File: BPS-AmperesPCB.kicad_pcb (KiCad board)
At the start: 2 copper layers, 58.2 x 30.2 mm, 32 parts, among them J1 ShuntConn, J2 LeaderConn, U1 AS8510-ASSM, U2 RO-123.3S_HP, U3 LTC6820, U4 HX1188FNL

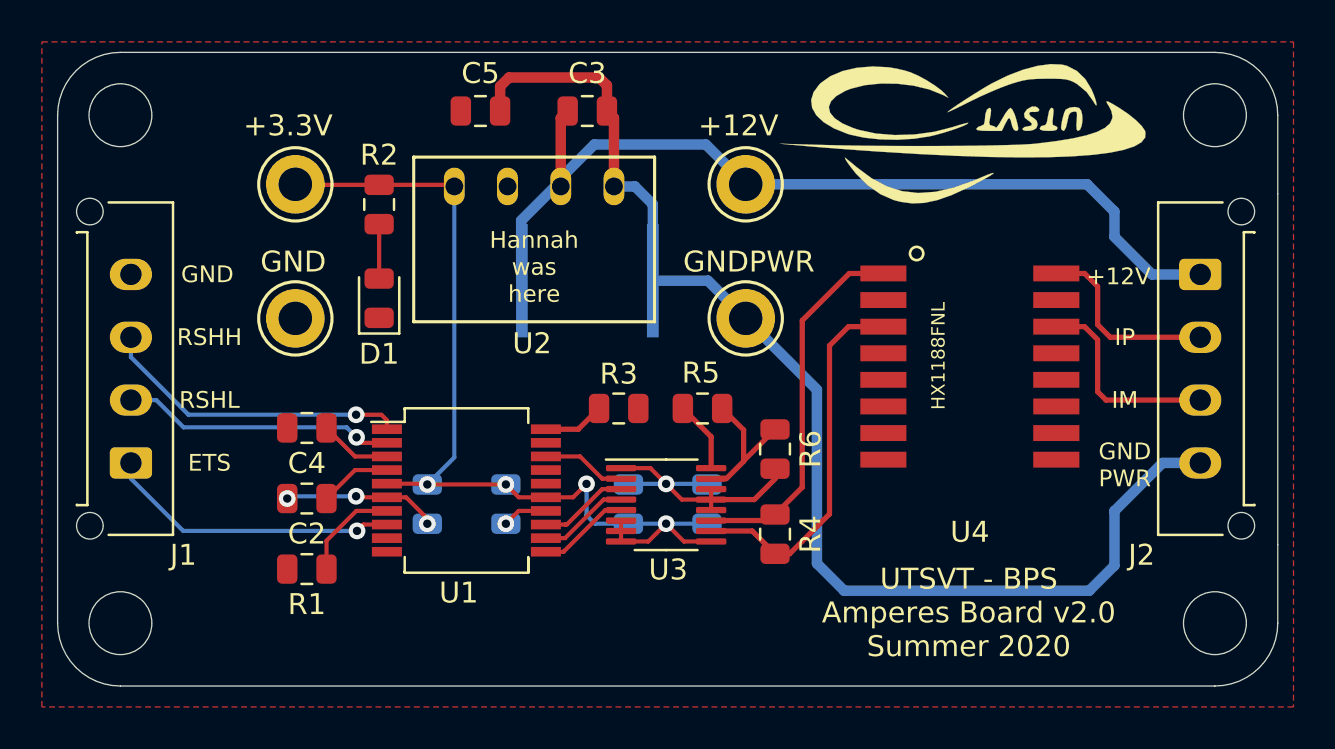
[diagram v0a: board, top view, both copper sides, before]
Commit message: Adds bottom gnd plane
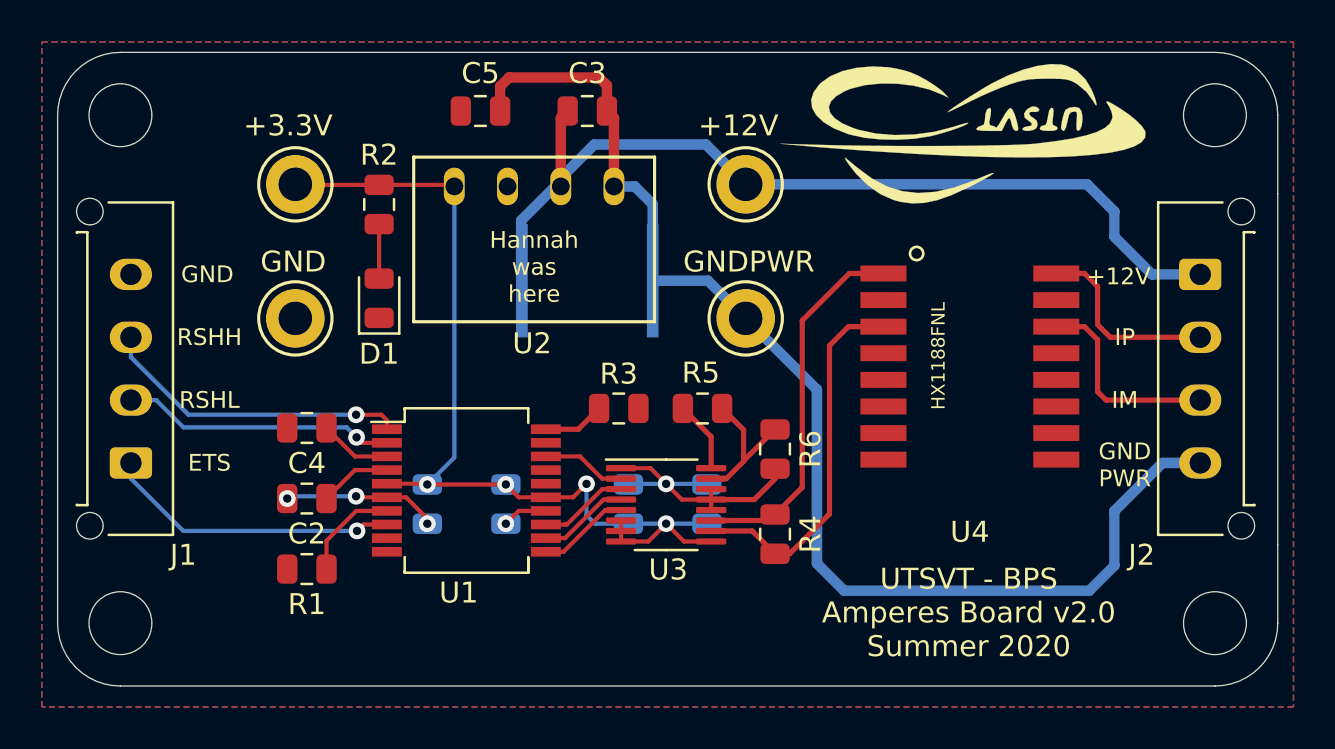
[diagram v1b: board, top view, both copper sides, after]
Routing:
- added copper zone on B.Cu, net GND
